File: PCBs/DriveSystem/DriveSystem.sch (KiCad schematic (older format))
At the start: 28 parts

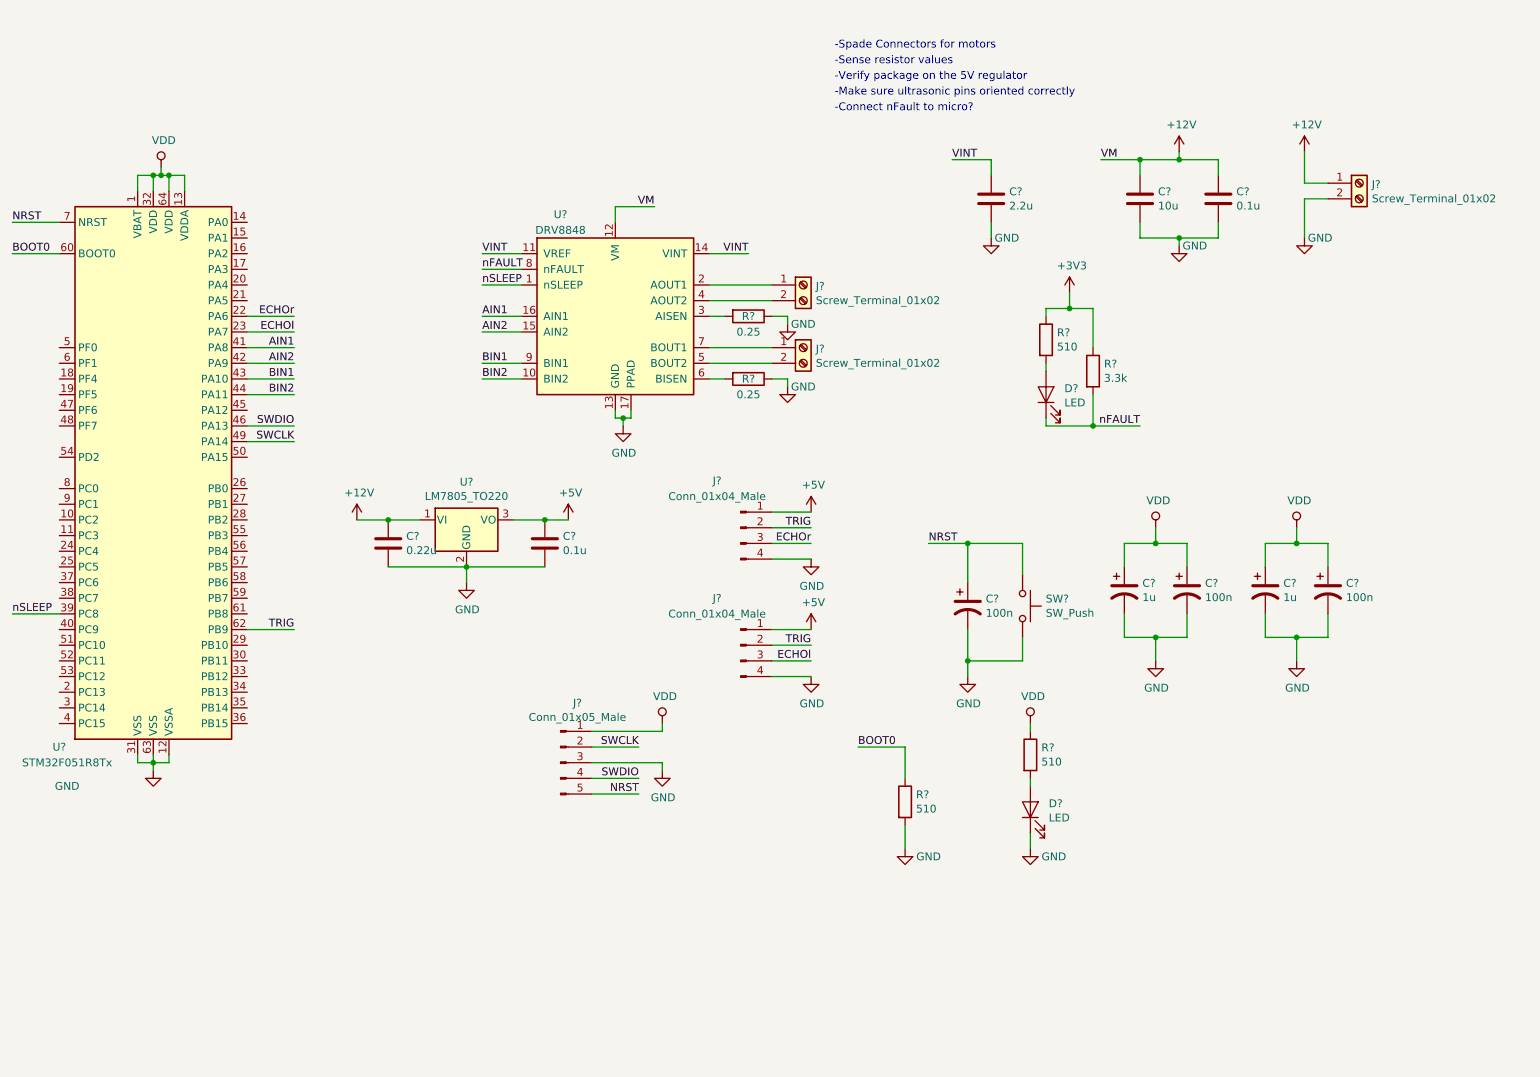
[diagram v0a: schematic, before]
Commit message: Added circuit descriptions
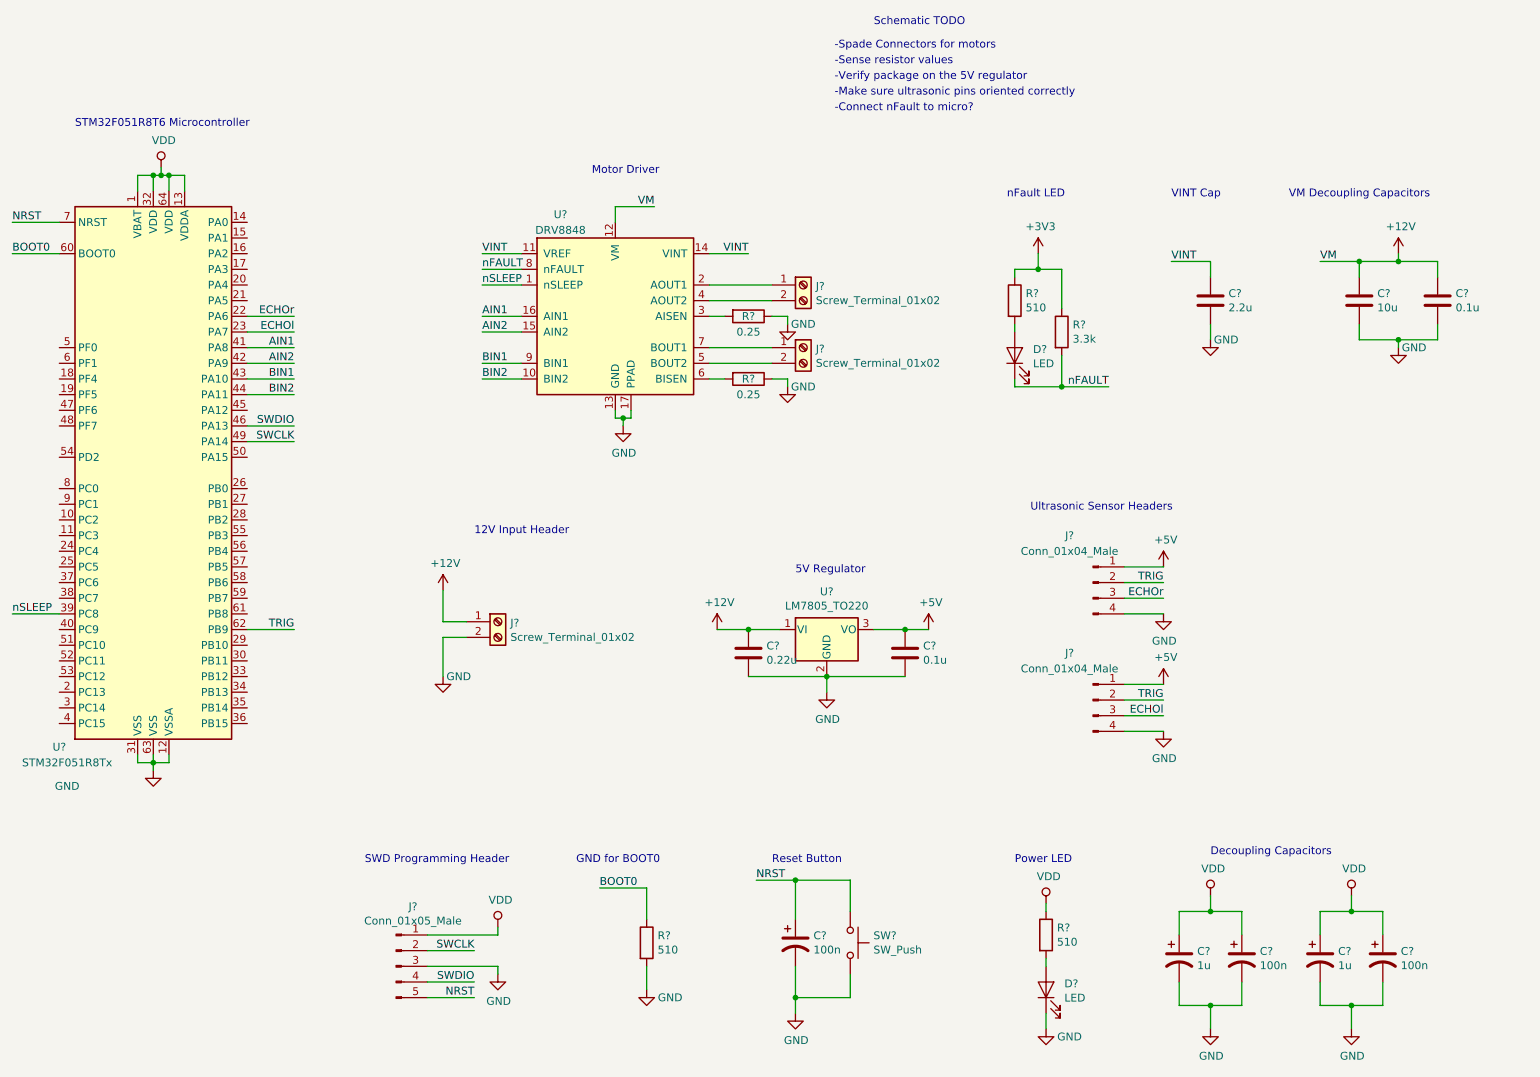
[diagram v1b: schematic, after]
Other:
- note added: "12V Input Header\n"
- note added: "5V Regulator\n"
- note added: "Decoupling Capacitors\n"
- note added: "GND for BOOT0\n"
- note added: "Motor Driver\n"
- note added: "Power LED\n"
- note added: "Reset Button\n"
- note added: "STM32F051R8T6 Microcontroller\n"
- note added: "SWD Programming Header\n"
- note added: "Schematic TODO\n"
- note added: "Ultrasonic Sensor Headers\n"
- note added: "VINT Cap\n"
- note added: "VM Decoupling Capacitors\n"
- note added: "nFault LED\n"
- moved on the sheet: C?, D?, J?, R?, SW?, U?

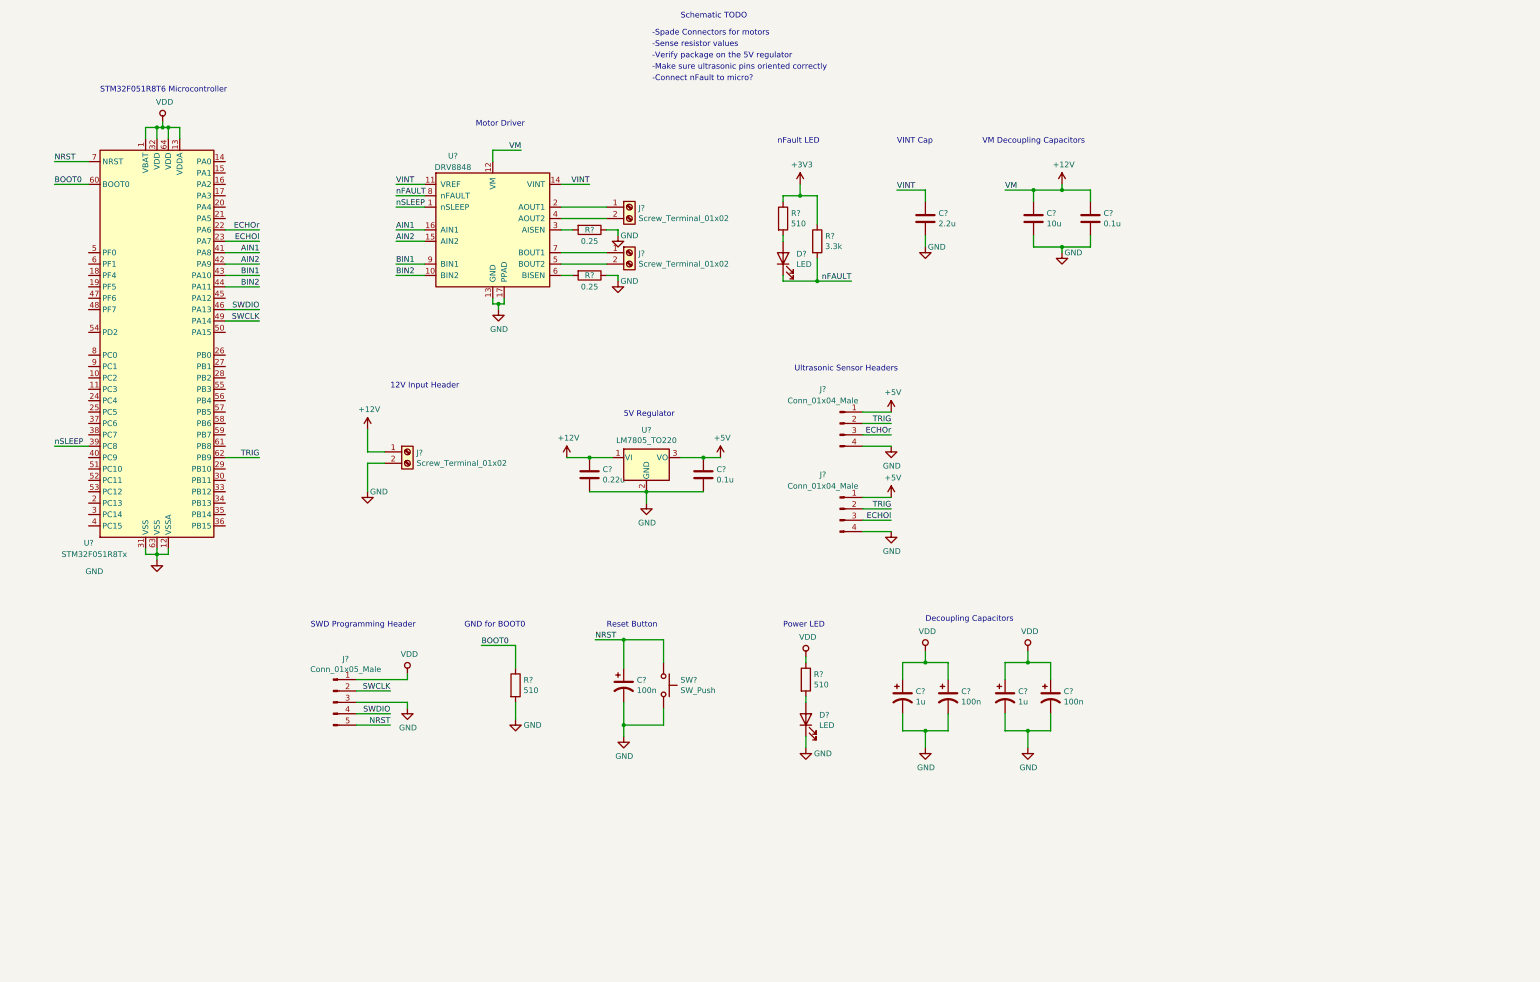
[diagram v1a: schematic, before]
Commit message: added touchscreen and stack light stuff
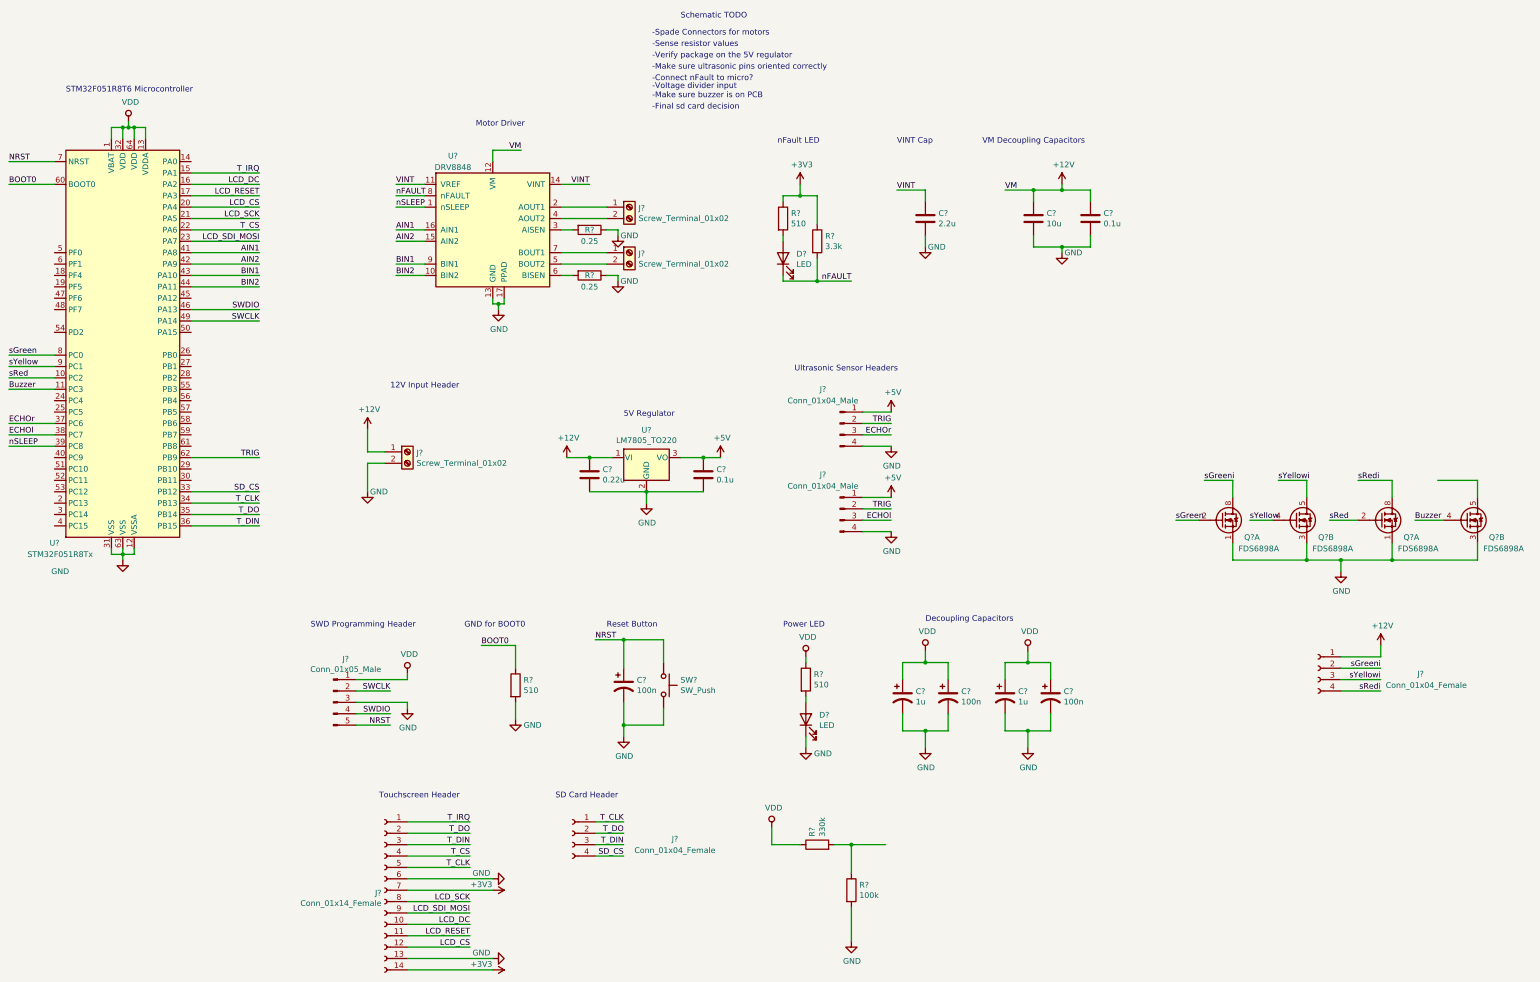
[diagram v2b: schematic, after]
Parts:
- added J?: Conn_01x14_Female, symbol Connector:Conn_01x14_Female
- added J? (x2): Conn_01x04_Female, symbol Connector:Conn_01x04_Female
- added Q? (x4): FDS6898A, Package_SO:SOIC-8_3.9x4.9mm_P1.27mm, symbol Transistor_FET:FDS6898A
- added R?: 330k, symbol Device:R
- added R?: 100k, symbol Device:R
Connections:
- net +12V: now also J?.1 (Pin_1)
- net +3V3: now also J?.14 (Pin_14), J?.7 (Pin_7)
- net ECHOl: now also U?.38 (PC7); no longer U?.23 (PA7)
- net ECHOr: now also U?.37 (PC6); no longer U?.22 (PA6)
- net GND: now also J?.13 (Pin_13), J?.6 (Pin_6), Q?.1 (S1), Q?.1 (S1), Q?.3 (S2), Q?.3 (S2), R?.2
- net VDD: now also R?.1
- net sRed: now reaches U?.10 (PC2)
- net sRed: now also Q?.2 (G1)
- net Buzzer: now reaches U?.11 (PC3)
- net Buzzer: now also Q?.4 (G2)
- net T_IRQ: now reaches U?.15 (PA1)
- net T_IRQ: now also J?.1 (Pin_1)
- net LCD_DC: now reaches U?.16 (PA2)
- net LCD_DC: now also J?.10 (Pin_10)
- net LCD_RESET: now reaches U?.17 (PA3)
- net LCD_RESET: now also J?.11 (Pin_11)
- net LCD_CS: now reaches U?.20 (PA4)
- net LCD_CS: now also J?.12 (Pin_12)
- net LCD_SCK: now reaches U?.21 (PA5)
- net LCD_SCK: now also J?.8 (Pin_8)
- net SD_CS: now reaches U?.33 (PB12)
- net SD_CS: now also J?.4 (Pin_4)
- net T_CLK: now reaches U?.34 (PB13)
- net T_CLK: now also J?.1 (Pin_1), J?.5 (Pin_5)
- net T_DO: now reaches U?.35 (PB14)
- net T_DO: now also J?.2 (Pin_2), J?.2 (Pin_2)
- net T_DIN: now reaches U?.36 (PB15)
- net T_DIN: now also J?.3 (Pin_3), J?.3 (Pin_3)
- net sGreen: now reaches U?.8 (PC0)
- net sGreen: now also Q?.2 (G1)
- net sYellow: now reaches U?.9 (PC1)
- net sYellow: now also Q?.4 (G2)
- new net: R?.1, R?.2
- new net: Q?.5 (D2), Q?.6 (D2)
- new net LCD_SDI_MOSI: J?.9 (Pin_9), U?.23 (PA7)
- new net T_CS: J?.4 (Pin_4), U?.22 (PA6)
- new net sGreeni: J?.2 (Pin_2), Q?.7 (D1), Q?.8 (D1)
- new net sRedi: J?.4 (Pin_4), Q?.7 (D1), Q?.8 (D1)
- new net sYellowi: J?.3 (Pin_3), Q?.5 (D2), Q?.6 (D2)
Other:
- note added: "-Final sd card decision\n"
- note added: "-Make sure buzzer is on PCB\n"
- note added: "-Voltage divider input\n\n"
- note added: "SD Card Header\n"
- note added: "Touchscreen Header\n"
- moved on the sheet: U?

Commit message: Added labels and notes
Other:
- note added: "-Add a switching 3v3 regulator to main (this) schematic\n"
- note added: "-Add header for LPS tag\n"
- note added: "-Add load cell / amp / header to the main circuit schematic"
- note added: "-Add servo controller / header to the main board\n"
- note added: "-Battery Input"
- note added: "-Battery charging circuit\n"
- note added: "-Battery measurement (voltage divider should be moved)\n"
- note added: "-IMU Header"
- note added: "-Maybe we multiplex the lights?"
- note added: "-Need to add our fat caps\n"
- note added: "-Terminals for the 12V output\n"
- note added: "-Terminals for the 12V regulator"
- note added: "Main Board\n"
- note added: "Power Distribution Board"
- note added: "Stack Light / Buzzer MOSFETs\n"
- note added: "Stack Light Header\n"
- note added: "What we need from Thomas:"
- moved on the sheet: C?, D?, J?, Q?A, Q?B, R?, SW?, U?
